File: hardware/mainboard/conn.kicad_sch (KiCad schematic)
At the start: 31 parts, among them J1 Conn_01x40_Shielded, J2 Conn_01x40_Shielded, J3 EAR, J4 Conn_02x06_Top_Bottom, P1 M2_SOCKET_E, SW1 SW_Push, SW2 SW_Push, U1 LIFCL_40_CABGA400, U10 Si52112-B, U9 74AHC1G126, Y1 25MHz

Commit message: More misc routing
Signed-off-by: David Shah <dave@ds0.me>
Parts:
- J4: symbol Connector_Generic:Conn_02x06_Top_Bottom -> Connector_Generic:Conn_02x06_Odd_Even
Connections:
- net +3V3: now also J4.11 (Pin_11); no longer J4.6 (Pin_6)
- net GND: now also J4.10 (Pin_10), J4.9 (Pin_9); no longer J4.11 (Pin_11), J4.5 (Pin_5)
- net PMOD1_10: now also J4.8 (Pin_8); no longer J4.10 (Pin_10)
- net PMOD1_2: now also J4.3 (Pin_3); no longer J4.2 (Pin_2)
- net PMOD1_3: now also J4.5 (Pin_5); no longer J4.3 (Pin_3)
- net PMOD1_4: now also J4.7 (Pin_7); no longer J4.4 (Pin_4)
- net PMOD1_7: now also J4.2 (Pin_2); no longer J4.7 (Pin_7)
- net PMOD1_8: now also J4.4 (Pin_4); no longer J4.8 (Pin_8)
- net PMOD1_9: now also J4.6 (Pin_6); no longer J4.9 (Pin_9)
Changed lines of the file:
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@@
     (pin "5")
   )
-  (symbol (lib_id "Connector_Generic:Conn_02x06_Top_Bottom") (at 220.98 182.88 0) (unit 1)
+  (symbol (lib_id "Connector_Generic:Conn_02x06_Odd_Even") (at 220.98 182.88 0) (unit 1)
     (in_bom yes) (on_board yes)
     (property "Reference" "J4" (id 0) (at 222.25 172.3198 0))

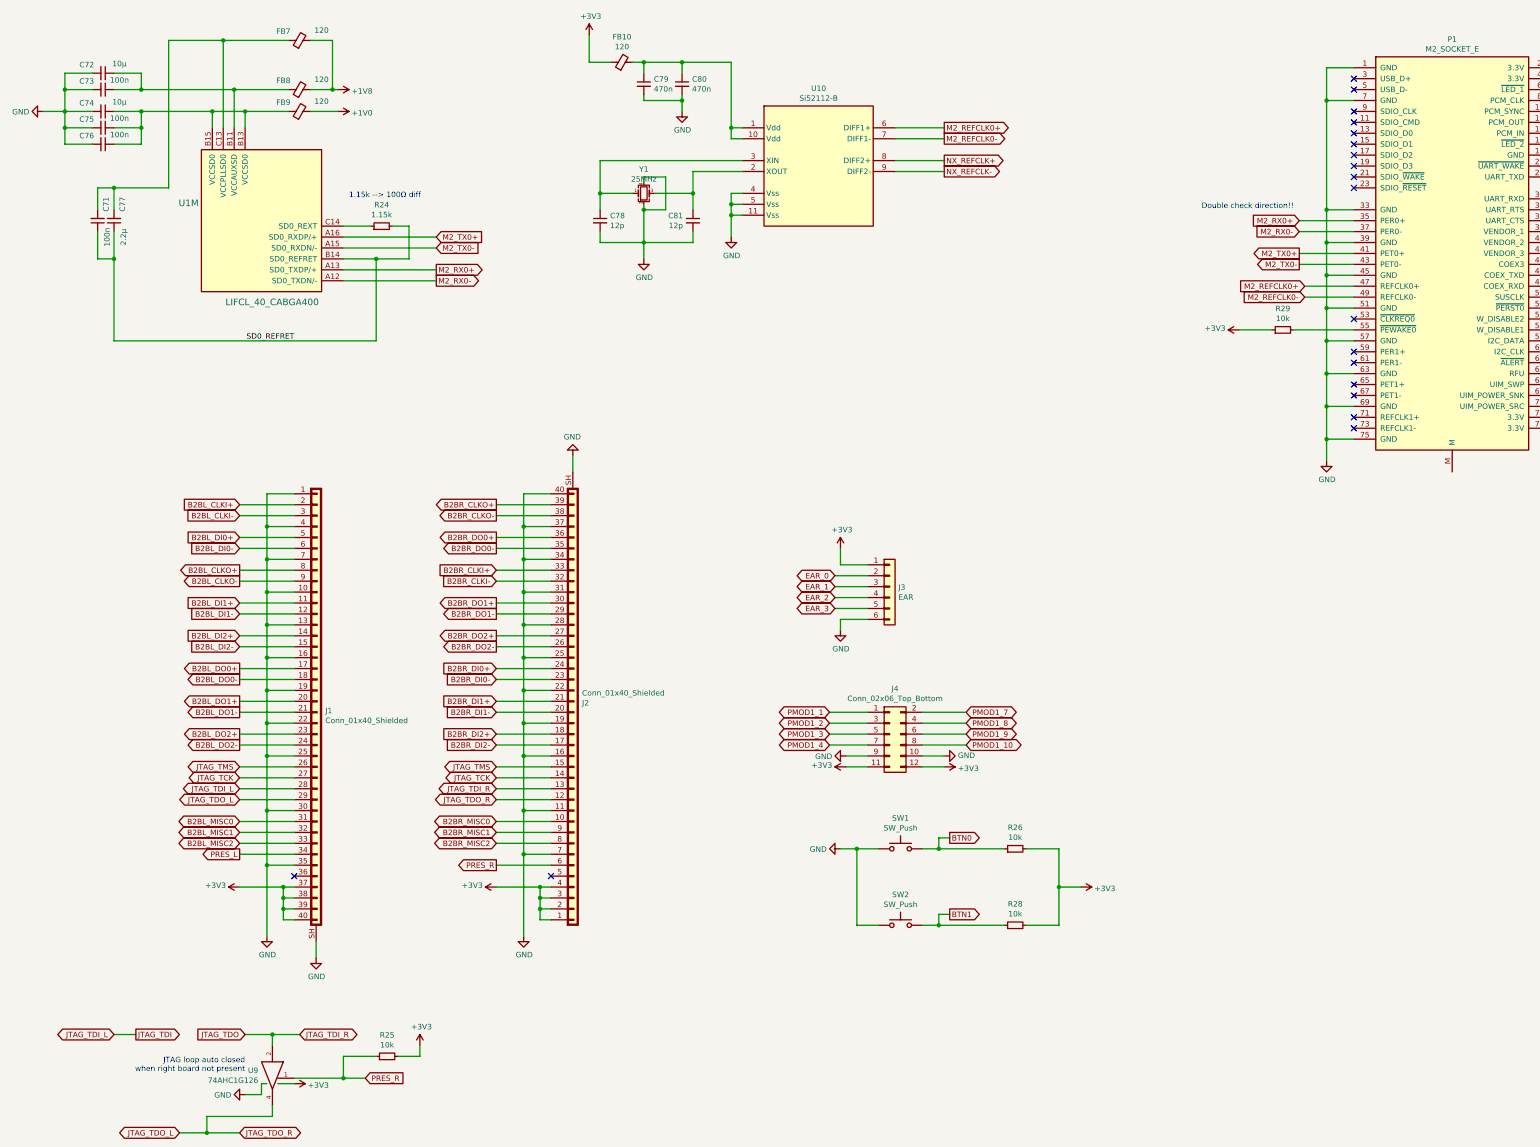
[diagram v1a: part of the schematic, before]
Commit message: mainboard: Fix some schematic ERC issues
Signed-off-by: gatecat <gatecat@ds0.me>
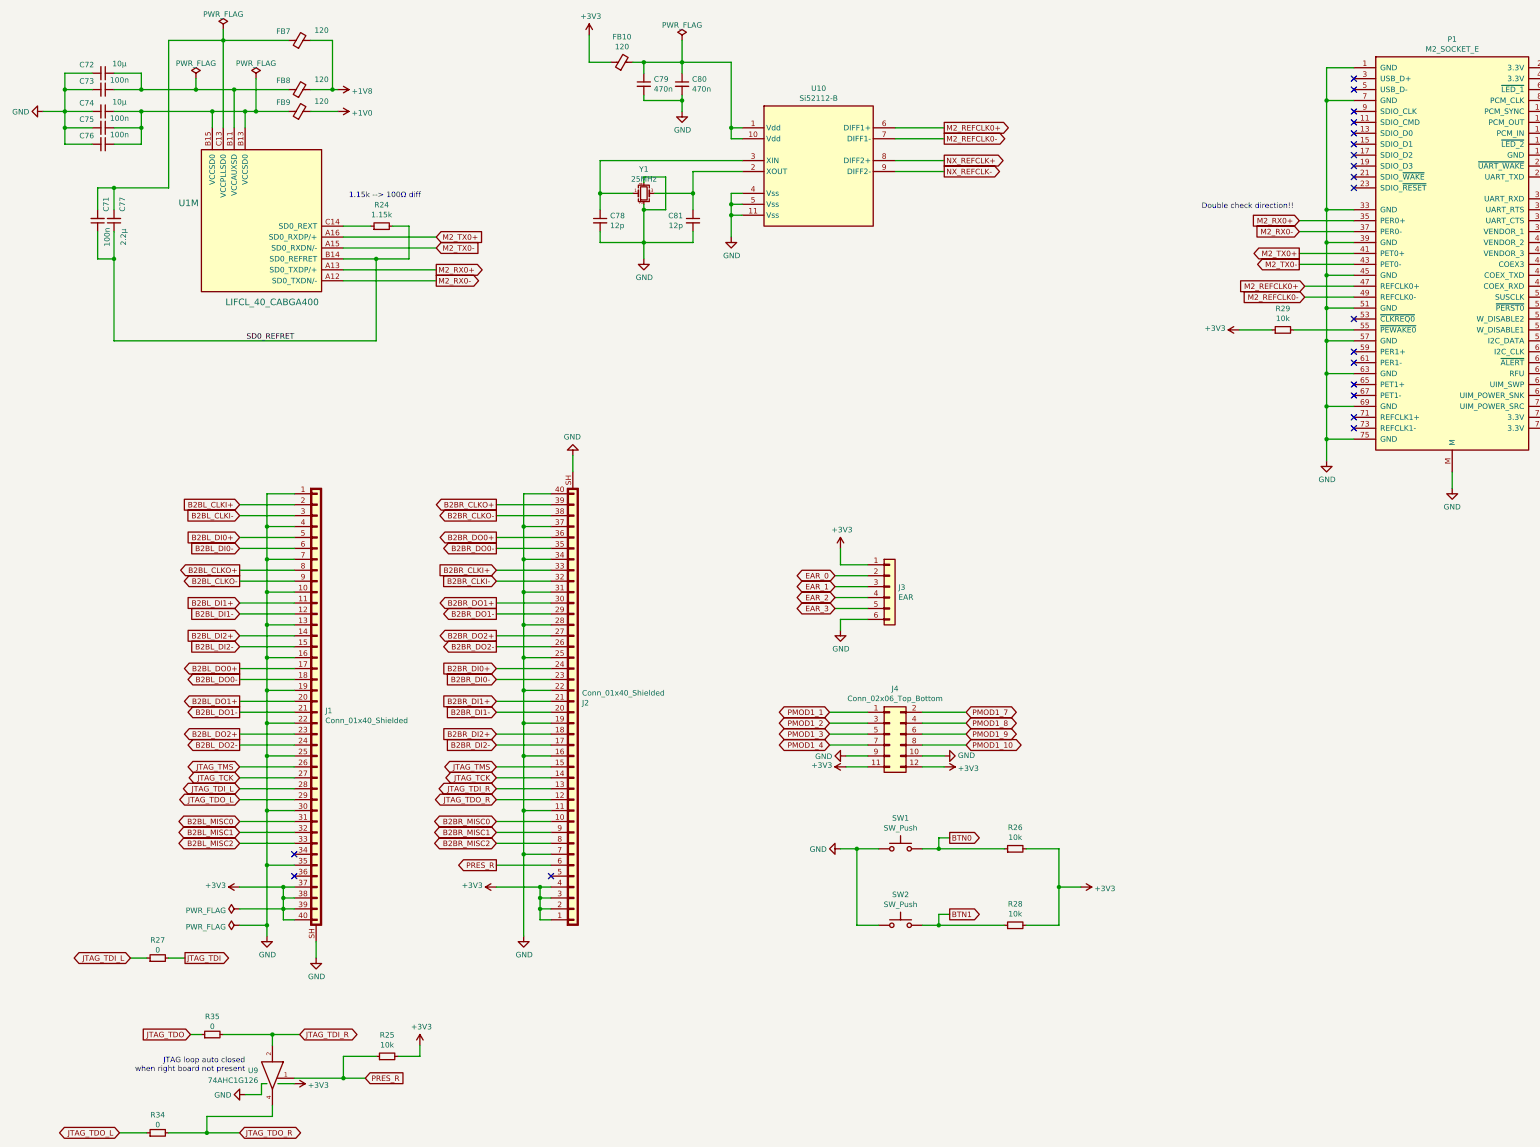
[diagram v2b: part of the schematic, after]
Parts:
- added R27, R34, R35: 0, Resistor_SMD:R_0402_1005Metric, symbol Device:R_Small
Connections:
- net GND: now also P1.M
- net JTAG_TDI: now also R27.2; no longer J1.28 (Pin_28)
- net JTAG_TDI_R: now also R35.2
- net JTAG_TDO_L: now also R34.1; no longer J2.12 (Pin_12), U9.4
- net PRES_L: no longer names the net of J1.34 (Pin_34)
- new net JTAG_TDI_L: J1.28 (Pin_28), R27.1
- new net JTAG_TDO: R35.1
- new net JTAG_TDO_R: J2.12 (Pin_12), R34.2, U9.4
- no-connect marks 43 -> 44

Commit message: Use B3U-3000P for all buttons
Signed-off-by: gatecat <gatecat@ds0.me>
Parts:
- SW1, SW2: footprint Button_Switch_THT:SW_Tactile_SPST_Angled_PTS645Vx31-2LFS -> Button_Switch_SMD:SW_SPST_B3U-3000P
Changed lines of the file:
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@@
     (property "Reference" "SW1" (id 0) (at 223.52 202.4188 0))
     (property "Value" "SW_Push" (id 1) (at 223.52 204.7175 0))
-    (property "Footprint" "Button_Switch_THT:SW_Tactile_SPST_Angled_PTS645Vx31-2LFS" (id 2) (at 223.52 204.47 0)
+    (property "Footprint" "Button_Switch_SMD:SW_SPST_B3U-3000P" (id 2) (at 223.52 204.47 0)
       (effects (font (size 1.27 1.27)) hide)
     )
@@
     (property "Reference" "SW2" (id 0) (at 223.52 220.199 0))
     (property "Value" "SW_Push" (id 1) (at 223.52 222.4975 0))
-    (property "Footprint" "Button_Switch_THT:SW_Tactile_SPST_Angled_PTS645Vx31-2LFS" (id 2) (at 223.52 222.25 0)
+    (property "Footprint" "Button_Switch_SMD:SW_SPST_B3U-3000P" (id 2) (at 223.52 222.25 0)
       (effects (font (size 1.27 1.27)) hide)
     )

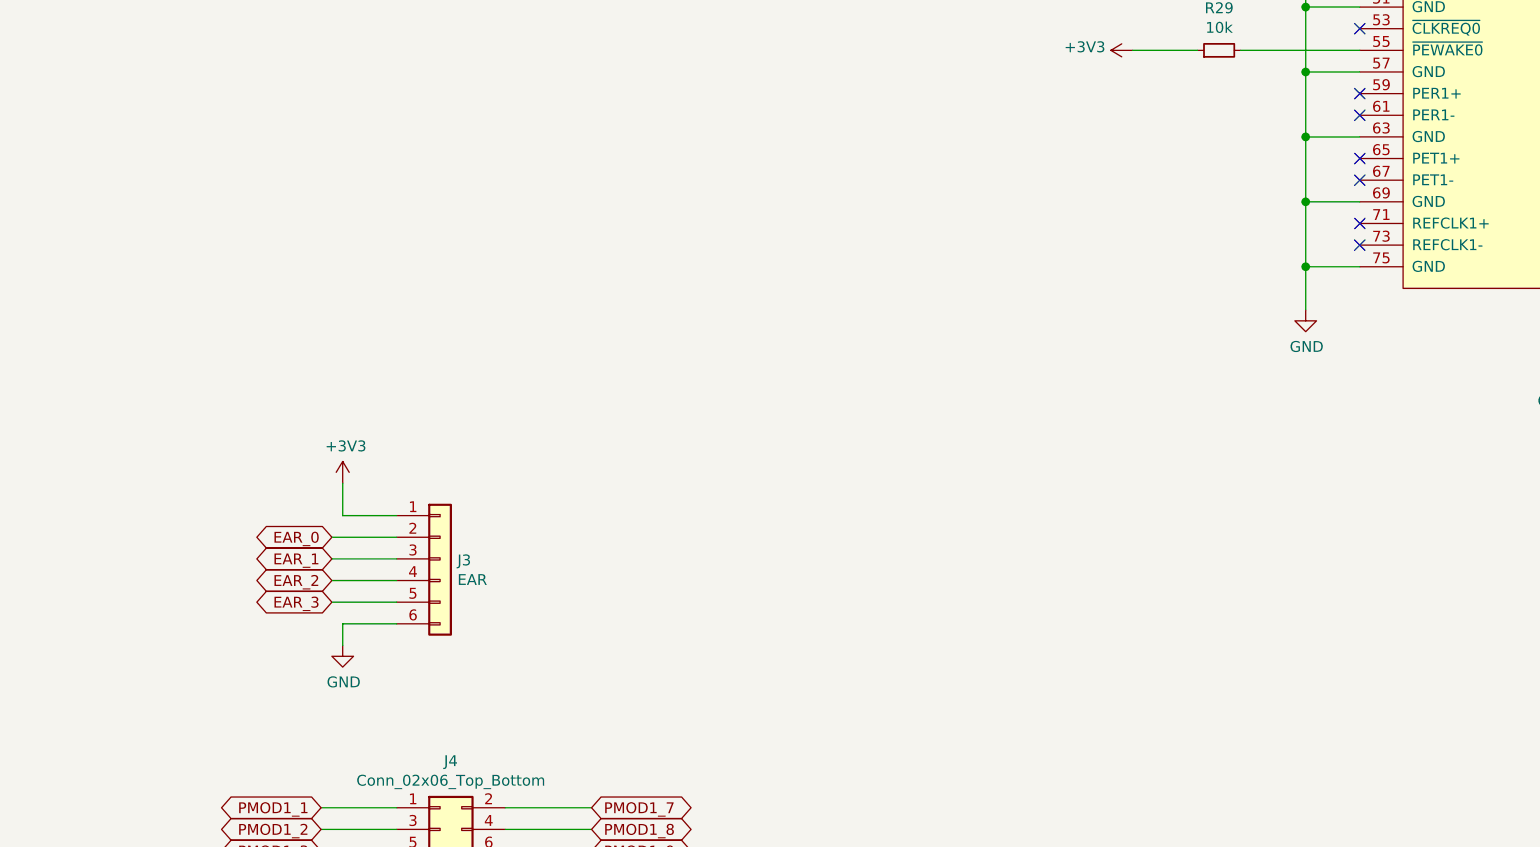
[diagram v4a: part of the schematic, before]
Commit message: Use 3-pin connector for ears
Signed-off-by: gatecat <gatecat@ds0.me>
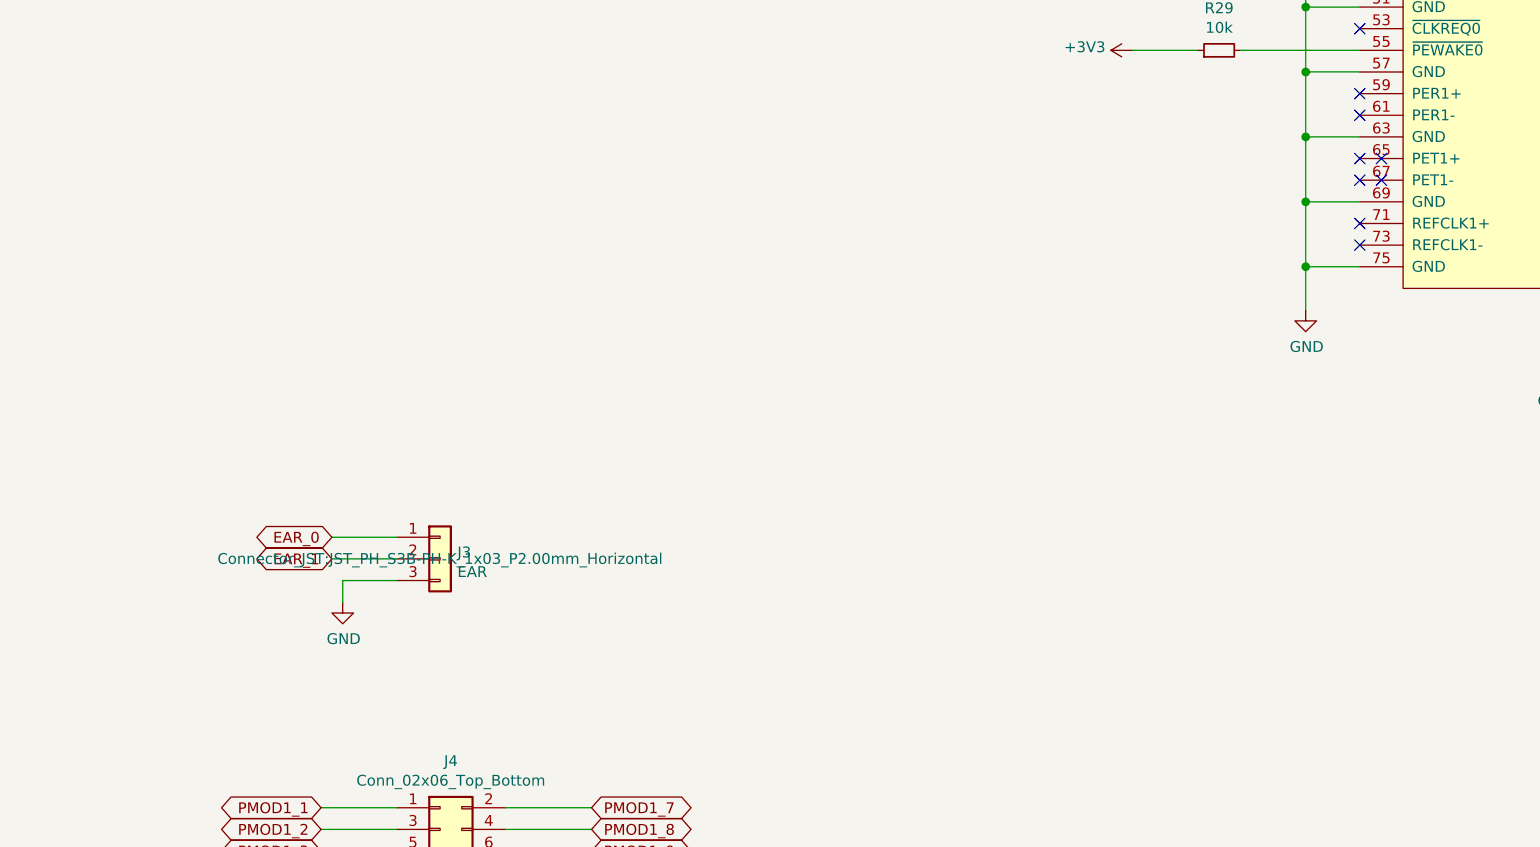
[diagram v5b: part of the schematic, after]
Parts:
- removed J3: EAR, Connector_PinHeader_2.00mm:PinHeader_2x03_P2.00mm_Horizontal, symbol Connector_Generic:Conn_01x06
- added J3: EAR, Connector_JST:JST_PH_S3B-PH-K_1x03_P2.00mm_Horizontal, symbol Connector_Generic:Conn_01x03
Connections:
- net EAR_0: now also J3.1 (Pin_1)
- net EAR_1: now also J3.2 (Pin_2)
- net GND: now also J3.3 (Pin_3)
- no-connect marks 44 -> 46
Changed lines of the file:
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@@
   (no_connect (at 328.93 109.22))
   (no_connect (at 328.93 111.76))
+  (no_connect (at 331.47 101.6))
+  (no_connect (at 331.47 104.14))
   (no_connect (at 374.65 33.02))
   (no_connect (at 374.65 35.56))
@@
     (stroke (width 0) (type solid) (color 0 0 0 0))
   )
-  (wire (pts (xy 208.28 151.13) (xy 215.9 151.13))
-    (stroke (width 0) (type solid) (color 0 0 0 0))
-  )
-  (wire (pts (xy 208.28 153.67) (xy 215.9 153.67))
-    (stroke (width 0) (type solid) (color 0 0 0 0))
-  )
-  (wire (pts (xy 209.55 143.51) (xy 209.55 139.7))
-    (stroke (width 0) (type solid) (color 0 0 0 0))
-  )
-  (wire (pts (xy 209.55 156.21) (xy 215.9 156.21))
-    (stroke (width 0) (type solid) (color 0 0 0 0))
-  )
-  (wire (pts (xy 209.55 158.75) (xy 209.55 156.21))
+  (wire (pts (xy 209.55 151.13) (xy 215.9 151.13))
+    (stroke (width 0) (type solid) (color 0 0 0 0))
+  )
+  (wire (pts (xy 209.55 153.67) (xy 209.55 151.13))
     (stroke (width 0) (type solid) (color 0 0 0 0))
   )
@@
   )
   (wire (pts (xy 213.36 209.55) (xy 218.44 209.55))
-    (stroke (width 0) (type solid) (color 0 0 0 0))
-  )
-  (wire (pts (xy 215.9 143.51) (xy 209.55 143.51))
     (stroke (width 0) (type solid) (color 0 0 0 0))
   )
@@
     )
   )
-  (global_label "EAR_2" (shape bidirectional) (at 208.28 151.13 180)
-    (effects (font (size 1.27 1.27)) (justify right))
-    (property "Intersheet References" "${INTERSHEET_REFS}" (id 0) (at 198.6581 151.0506 0)
-      (effects (font (size 1.27 1.27)) (justify right) hide)
-    )
-  )
-  (global_label "EAR_3" (shape bidirectional) (at 208.28 153.67 180)
-    (effects (font (size 1.27 1.27)) (justify right))
-    (property "Intersheet References" "${INTERSHEET_REFS}" (id 0) (at 198.6581 153.5906 0)
-      (effects (font (size 1.27 1.27)) (justify right) hide)
-    )
-  )
   (global_label "M2_REFCLK0+" (shape output) (at 233.68 41.91 0)
     (effects (font (size 1.27 1.27)) (justify left))
@@
     (pin "1")
   )
-  (symbol (lib_id "power:+3V3") (at 209.55 139.7 0) (unit 1)
-    (in_bom yes) (on_board yes)
-    (property "Reference" "#PWR096" (id 0) (at 209.55 143.51 0)
-      (effects (font (size 1.27 1.27)) hide)
-    )
-    (property "Value" "+3V3" (id 1) (at 209.9183 135.3756 0))
-    (property "Footprint" "" (id 2) (at 209.55 139.7 0)
-      (effects (font (size 1.27 1.27)) hide)
-    )
-    (property "Datasheet" "" (id 3) (at 209.55 139.7 0)
-      (effects (font (size 1.27 1.27)) hide)
-    )
-    (pin "1")
-  )
   (symbol (lib_id "power:+3V3") (at 210.82 190.5 90) (unit 1)
     (in_bom yes) (on_board yes)
@@
     (pin "1")
   )
-  (symbol (lib_id "power:GND") (at 209.55 158.75 0) (unit 1)
-    (in_bom yes) (on_board yes)
-    (property "Reference" "#PWR097" (id 0) (at 209.55 165.1 0)
-      (effects (font (size 1.27 1.27)) hide)
-    )
-    (property "Value" "GND" (id 1) (at 209.6643 163.0744 0))
-    (property "Footprint" "" (id 2) (at 209.55 158.75 0)
-      (effects (font (size 1.27 1.27)) hide)
-    )
-    (property "Datasheet" "" (id 3) (at 209.55 158.75 0)
+  (symbol (lib_id "power:GND") (at 209.55 153.67 0) (unit 1)
+    (in_bom yes) (on_board yes)
+    (property "Reference" "#PWR097" (id 0) (at 209.55 160.02 0)
+      (effects (font (size 1.27 1.27)) hide)
+    )
+    (property "Value" "GND" (id 1) (at 209.6643 157.9944 0))
+    (property "Footprint" "" (id 2) (at 209.55 153.67 0)
+      (effects (font (size 1.27 1.27)) hide)
+    )
+    (property "Datasheet" "" (id 3) (at 209.55 153.67 0)
       (effects (font (size 1.27 1.27)) hide)
     )
@@
     (pin "2")
   )
-  (symbol (lib_id "Connector_Generic:Conn_01x06") (at 220.98 148.59 0) (unit 1)
-    (in_bom yes) (on_board yes)
-    (property "Reference" "J3" (id 0) (at 223.0121 148.7614 0)
+  (symbol (lib_id "Connector_Generic:Conn_01x03") (at 220.98 148.59 0) (unit 1)
+    (in_bom yes) (on_board yes)
+    (property "Reference" "J3" (id 0) (at 223.0121 147.8291 0)
       (effects (font (size 1.27 1.27)) (justify left))
     )
-    (property "Value" "EAR" (id 1) (at 223.012 151.06 0)
+    (property "Value" "EAR" (id 1) (at 223.0121 150.1278 0)
       (effects (font (size 1.27 1.27)) (justify left))
     )
-    (property "Footprint" "Connector_PinHeader_2.00mm:PinHeader_2x03_P2.00mm_Horizontal" (id 2) (at 220.98 148.59 0)
-      (effects (font (size 1.27 1.27)) hide)
-    )
+    (property "Footprint" "Connector_JST:JST_PH_S3B-PH-K_1x03_P2.00mm_Horizontal" (id 2) (at 220.98 148.59 0))
     (property "Datasheet" "~" (id 3) (at 220.98 148.59 0)
       (effects (font (size 1.27 1.27)) hide)
@@
     (pin "2")
     (pin "3")
-    (pin "4")
-    (pin "5")
-    (pin "6")
   )
   (symbol (lib_id "74xGxx:74AHC1G126") (at 77.47 262.89 270) (unit 1)

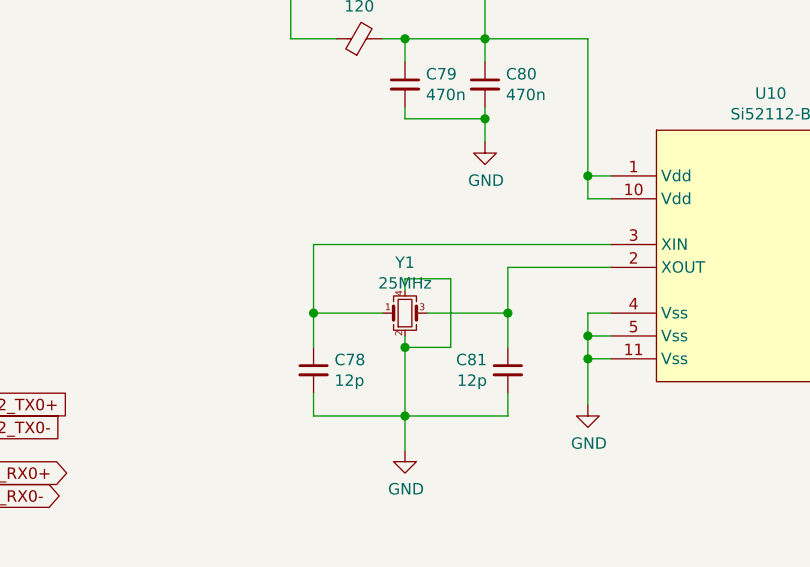
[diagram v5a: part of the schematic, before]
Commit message: Update some part numbers
Signed-off-by: gatecat <gatecat@ds0.me>
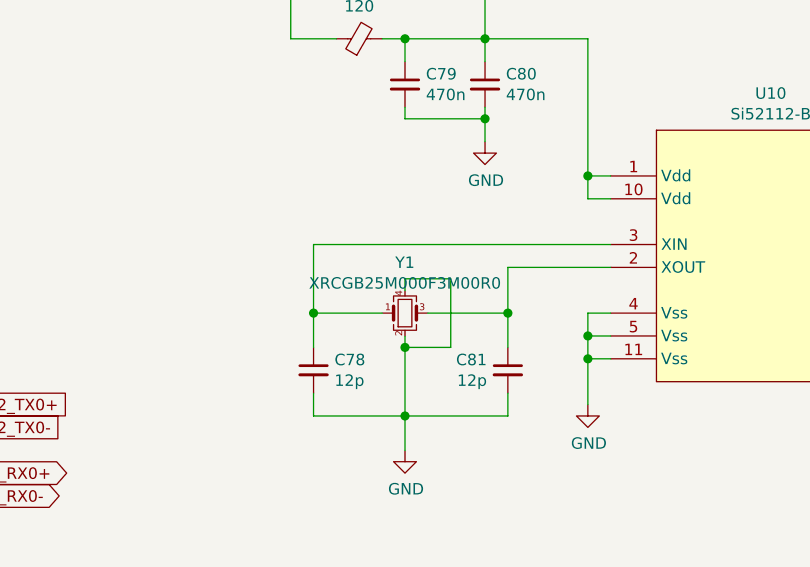
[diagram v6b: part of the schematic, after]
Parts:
- Y1: value 25MHz -> XRCGB25M000F3M00R0
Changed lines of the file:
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@@
     (in_bom yes) (on_board yes)
     (property "Reference" "Y1" (id 0) (at 163.83 51.5428 0))
-    (property "Value" "25MHz" (id 1) (at 163.83 53.841 0))
+    (property "Value" "XRCGB25M000F3M00R0" (id 1) (at 163.83 53.841 0))
     (property "Footprint" "Crystal:Crystal_SMD_2016-4Pin_2.0x1.6mm" (id 2) (at 163.83 57.15 0)
       (effects (font (size 1.27 1.27)) hide)
